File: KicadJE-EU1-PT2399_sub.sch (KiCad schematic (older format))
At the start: 49 parts, among them J201 In, J202 Out, P201 HEADER_2x5_Doepfer, Q201 BC337, Q202 PZT2222A, Q203 PZT2222A, U202 PT2399

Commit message: argh Kicad not stable
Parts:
- D204: footprint Diode_SMD:D_MELF-RM10_Universal_Handsoldering -> Diode_SMD:D_MiniMELF
- RV202: footprint Potentiometer_THT:Potentiometer_Alps_RK09K_Single_Vertical -> Potentiometer_THT:Potentiometer_China_RK09_Single_Vertical_AJ
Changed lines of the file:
@@
 F 0 "D204" V 4004 1704 50  0000 L CNN
 F 1 "5v6" V 4095 1704 50  0000 L CNN
-F 2 "Diode_SMD:D_MELF-RM10_Universal_Handsoldering" H 4050 1625 50  0001 C CNN
+F 2 "Diode_SMD:D_MiniMELF" H 4050 1625 50  0001 C CNN
 F 3 "~" H 4050 1625 50  0001 C CNN
 	1    4050 1625
@@
 F 0 "RV202" H 2380 5071 50  0000 R CNN
 F 1 "20k" H 2380 4980 50  0000 R CNN
-F 2 "Potentiometer_THT:Potentiometer_Alps_RK09K_Single_Vertical" H 2450 5025 50  0001 C CNN
+F 2 "Potentiometer_THT:Potentiometer_China_RK09_Single_Vertical_AJ" H 2450 5025 50  0001 C CNN
 F 3 "~" H 2450 5025 50  0001 C CNN
 	1    2450 5025

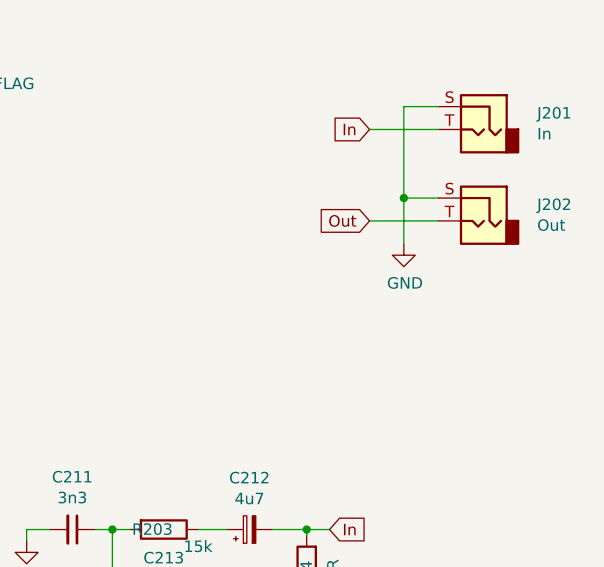
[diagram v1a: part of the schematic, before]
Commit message: Components placed on PT2399
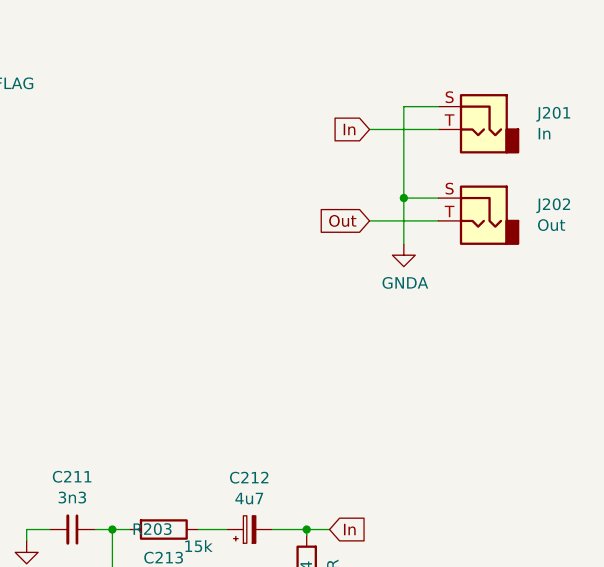
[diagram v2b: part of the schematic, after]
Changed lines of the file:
@@
 Wire Wire Line
 	6675 1200 6675 1600
-$Comp
-L power:GND #PWR?
-U 1 1 5C68B7E3
-P 6675 1800
-AR Path="/5C68B7E3" Ref="#PWR?"  Part="1"
-AR Path="/5D60ED9A/5C68B7E3" Ref="#PWR0205"  Part="1"
-F 0 "#PWR0205" H 6675 1550 50  0001 C CNN
-F 1 "GND" H 6680 1627 50  0000 C CNN
-F 2 "" H 6675 1800 50  0001 C CNN
-F 3 "" H 6675 1800 50  0001 C CNN
-	1    6675 1800
-	1    0    0    -1
-$EndComp
 Text GLabel 6525 1300 0    50   Input ~ 0
 In
@@
 Wire Wire Line
 	1875 1450 2550 1450
+$Comp
+L power:GNDA #PWR?
+U 1 1 5C768062
+P 6675 1800
+F 0 "#PWR?" H 6675 1550 50  0001 C CNN
+F 1 "GNDA" H 6680 1627 50  0000 C CNN
+F 2 "" H 6675 1800 50  0001 C CNN
+F 3 "" H 6675 1800 50  0001 C CNN
+	1    6675 1800
+	1    0    0    -1
+$EndComp
 $EndSCHEMATC

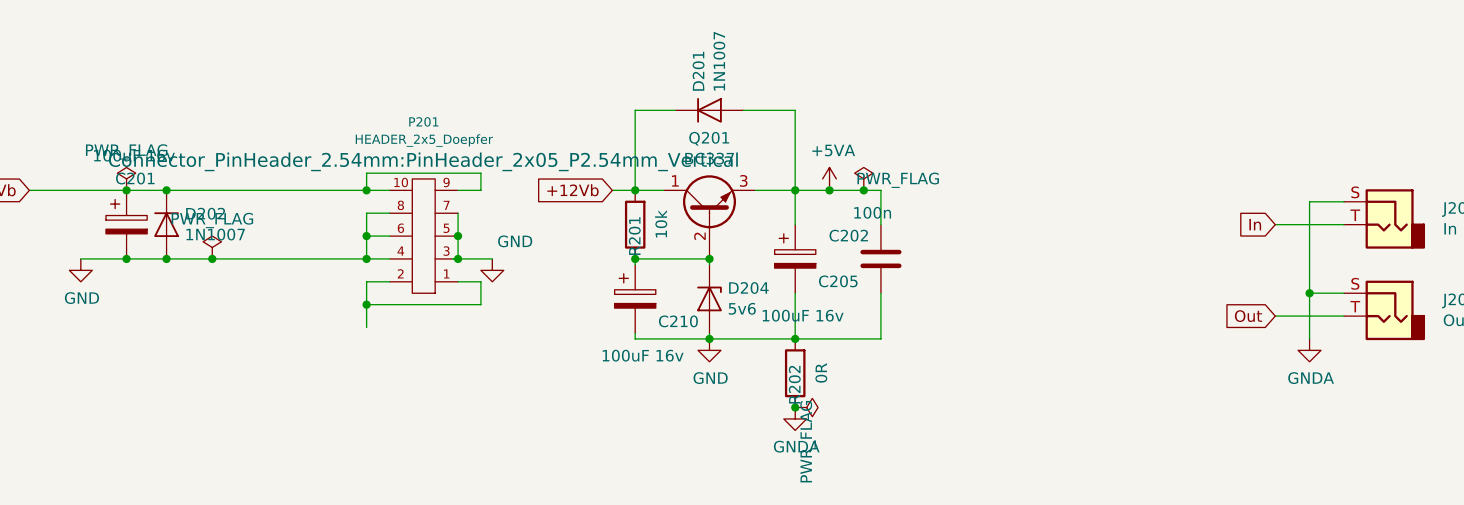
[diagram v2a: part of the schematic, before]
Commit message: Added 78L05 reg
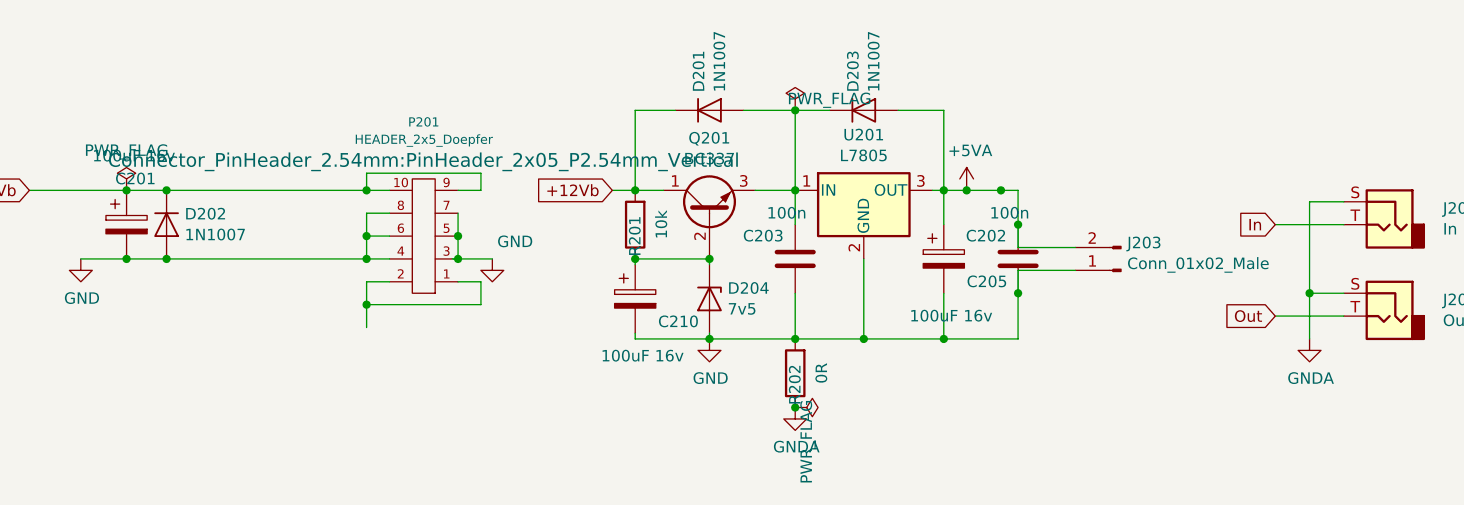
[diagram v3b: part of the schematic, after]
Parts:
- added C203: 100n, Capacitor_SMD:C_0805_2012Metric_Pad1.15x1.40mm_HandSolder, symbol Device:C
- added D203: 1N1007, Diode_SMD:D_SOD-123, symbol Device:D
- added J203: Conn_01x02_Male, Connector_PinHeader_2.54mm:PinHeader_1x02_P2.54mm_Vertical, symbol Connector:Conn_01x02_Male
- added U201: L7805, Package_TO_SOT_THT:TO-92, symbol Envelope-cache-2018-08-04-13-00-04:L7805
- D204: value 5v6 -> 7v5
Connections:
- wire segments 137 -> 149
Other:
- moved on the sheet: C202, C205
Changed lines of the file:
@@
 L Device:C C?
 U 1 1 5D62F383
-P 4800 1450
+P 5400 1450
 AR Path="/5D62F383" Ref="C?"  Part="1"
 AR Path="/5D60ED9A/5D62F383" Ref="C202"  Part="1"
-F 0 "C202" H 4850 1350 50  0000 L CNN
-F 1 "100n" H 4750 1250 50  0000 L CNN
-F 2 "Capacitor_SMD:C_0805_2012Metric_Pad1.15x1.40mm_HandSolder" H 4838 1300 50  0001 C CNN
-F 3 "~" H 4800 1450 50  0001 C CNN
-	1    4800 1450
+F 0 "C202" H 5450 1350 50  0000 L CNN
+F 1 "100n" H 5350 1250 50  0000 L CNN
+F 2 "Capacitor_SMD:C_0805_2012Metric_Pad1.15x1.40mm_HandSolder" H 5438 1300 50  0001 C CNN
+F 3 "~" H 5400 1450 50  0001 C CNN
+	1    5400 1450
 	-1   0    0    1
 $EndComp
@@
 	1    0    0    -1
 $EndComp
-$Comp
-L power:PWR_FLAG #FLG?
-U 1 1 5D62F3D0
-P 1875 1450
-AR Path="/5D62F3D0" Ref="#FLG?"  Part="1"
-AR Path="/5D60ED9A/5D62F3D0" Ref="#FLG0203"  Part="1"
-F 0 "#FLG0203" H 1875 1525 50  0001 C CNN
-F 1 "PWR_FLAG" H 1875 1624 50  0000 C CNN
-F 2 "" H 1875 1450 50  0001 C CNN
-F 3 "~" H 1875 1450 50  0001 C CNN
-	1    1875 1450
-	1    0    0    -1
-$EndComp
 Text GLabel 1075 1150 0    50   Input ~ 0
 +12Vb
@@
 L Device:CP C?
 U 1 1 5D645B0A
-P 4425 1450
+P 5075 1450
 AR Path="/5D645B0A" Ref="C?"  Part="1"
 AR Path="/5D60ED9A/5D645B0A" Ref="C205"  Part="1"
-F 0 "C205" H 4525 1350 50  0000 L CNN
-F 1 "100uF 16v" H 4275 1200 50  0000 L CNN
-F 2 "Capacitor_THT:CP_Radial_D5.0mm_P2.50mm" H 4463 1300 50  0001 C CNN
-F 3 "~" H 4425 1450 50  0001 C CNN
-	1    4425 1450
+F 0 "C205" H 5175 1350 50  0000 L CNN
+F 1 "100uF 16v" H 4925 1200 50  0000 L CNN
+F 2 "Capacitor_THT:CP_Radial_D5.0mm_P2.50mm" H 5113 1300 50  0001 C CNN
+F 3 "~" H 5075 1450 50  0001 C CNN
+	1    5075 1450
 	1    0    0    -1
 $EndComp
@@
 P 4050 1625
 F 0 "D204" V 4004 1704 50  0000 L CNN
-F 1 "5v6" V 4095 1704 50  0000 L CNN
+F 1 "7v5" V 4095 1704 50  0000 L CNN
 F 2 "Diode_SMD:D_MiniMELF" H 4050 1625 50  0001 C CNN
 F 3 "~" H 4050 1625 50  0001 C CNN
@@
 L power:+5VA #PWR0201
 U 1 1 5D64AB64
-P 4575 1150
-F 0 "#PWR0201" H 4575 1000 50  0001 C CNN
-F 1 "+5VA" H 4590 1323 50  0000 C CNN
-F 2 "" H 4575 1150 50  0001 C CNN
-F 3 "" H 4575 1150 50  0001 C CNN
-	1    4575 1150
+P 5175 1150
+F 0 "#PWR0201" H 5175 1000 50  0001 C CNN
+F 1 "+5VA" H 5190 1323 50  0000 C CNN
+F 2 "" H 5175 1150 50  0001 C CNN
+F 3 "" H 5175 1150 50  0001 C CNN
+	1    5175 1150
 	1    0    0    -1
 $EndComp
@@
 L power:PWR_FLAG #FLG?
 U 1 1 5D64AB9E
-P 4725 1150
+P 4425 800
 AR Path="/5D64AB9E" Ref="#FLG?"  Part="1"
 AR Path="/5D60ED9A/5D64AB9E" Ref="#FLG0202"  Part="1"
-F 0 "#FLG0202" H 4725 1225 50  0001 C CNN
-F 1 "PWR_FLAG" H 4875 1200 50  0000 C CNN
-F 2 "" H 4725 1150 50  0001 C CNN
-F 3 "~" H 4725 1150 50  0001 C CNN
-	1    4725 1150
+F 0 "#FLG0202" H 4425 875 50  0001 C CNN
+F 1 "PWR_FLAG" H 4575 850 50  0000 C CNN
+F 2 "" H 4425 800 50  0001 C CNN
+F 3 "~" H 4425 800 50  0001 C CNN
+	1    4425 800
 	1    0    0    -1
 $EndComp
@@
 	3625 1150 3725 1150
 Wire Wire Line
-	4425 1150 4575 1150
-Connection ~ 4575 1150
-Wire Wire Line
-	4575 1150 4725 1150
+	5025 1150 5075 1150
+Connection ~ 5175 1150
+Wire Wire Line
+	5175 1150 5325 1150
 $Comp
 L Audio:PT2399 U202
@@
 	1075 1150 1500 1150
 Wire Wire Line
-	4425 1800 4800 1800
-Wire Wire Line
-	4800 1800 4800 1600
-Wire Wire Line
 	1675 1150 2550 1150
 Wire Wire Line
-	1675 1450 1875 1450
-Wire Wire Line
-	4800 1300 4800 1150
-Wire Wire Line
-	4800 1150 4725 1150
-Connection ~ 4725 1150
-Connection ~ 1875 1450
-Wire Wire Line
-	1875 1450 2550 1450
-$Comp
-L power:GNDA #PWR?
+	5400 1150 5325 1150
+Connection ~ 5325 1150
+$Comp
+L power:GNDA #PWR0102
 U 1 1 5C768062
 P 6675 1800
-F 0 "#PWR?" H 6675 1550 50  0001 C CNN
+F 0 "#PWR0102" H 6675 1550 50  0001 C CNN
 F 1 "GNDA" H 6680 1627 50  0000 C CNN
 F 2 "" H 6675 1800 50  0001 C CNN
@@
 	1    0    0    -1
 $EndComp
+$Comp
+L Connector:Conn_01x02_Male J203
+U 1 1 5C76AAB7
+P 5850 1500
+F 0 "J203" H 5823 1380 50  0000 R CNN
+F 1 "Conn_01x02_Male" H 5823 1471 50  0000 R CNN
+F 2 "Connector_PinHeader_2.54mm:PinHeader_1x02_P2.54mm_Vertical" H 5850 1500 50  0001 C CNN
+F 3 "~" H 5850 1500 50  0001 C CNN
+	1    5850 1500
+	-1   0    0    1
+$EndComp
+$Comp
+L Envelope-cache-2018-08-04-13-00-04:L7805 U201
+U 1 1 5C76AC9D
+P 4725 1150
+F 0 "U201" H 4725 1392 50  0000 C CNN
+F 1 "L7805" H 4725 1301 50  0000 C CNN
+F 2 "Package_TO_SOT_THT:TO-92" H 4750 1000 50  0001 L CIN
+F 3 "" H 4725 1100 50  0001 C CNN
+	1    4725 1150
+	1    0    0    -1
+$EndComp
+Wire Wire Line
+	5075 1300 5075 1150
+Connection ~ 5075 1150
+Wire Wire Line
+	5075 1150 5175 1150
+Wire Wire Line
+	5075 1600 5075 1800
+Connection ~ 5075 1800
+Wire Wire Line
+	5075 1800 5400 1800
+Wire Wire Line
+	4425 1800 4725 1800
+$Comp
+L Device:C C?
+U 1 1 5C78460D
+P 4425 1450
+AR Path="/5C78460D" Ref="C?"  Part="1"
+AR Path="/5D60ED9A/5C78460D" Ref="C203"  Part="1"
+F 0 "C203" H 4475 1350 50  0000 L CNN
+F 1 "100n" H 4375 1250 50  0000 L CNN
+F 2 "Capacitor_SMD:C_0805_2012Metric_Pad1.15x1.40mm_HandSolder" H 4463 1300 50  0001 C CNN
+F 3 "~" H 4425 1450 50  0001 C CNN
+	1    4425 1450
+	-1   0    0    1
+$EndComp
+Wire Wire Line
+	4725 1450 4725 1800
+Connection ~ 4725 1800
+Wire Wire Line
+	4725 1800 5075 1800
+Wire Wire Line
+	5400 1400 5650 1400
+Wire Wire Line
+	5400 1150 5400 1300
+Connection ~ 5400 1300
+Wire Wire Line
+	5400 1300 5400 1400
+Wire Wire Line
+	5650 1500 5400 1500
+Wire Wire Line
+	5400 1500 5400 1600
+Connection ~ 5400 1600
+Wire Wire Line
+	5400 1600 5400 1800
+$Comp
+L Device:D D?
+U 1 1 5C794D49
+P 4725 800
+AR Path="/5C794D49" Ref="D?"  Part="1"
+AR Path="/5D60ED9A/5C794D49" Ref="D203"  Part="1"
+F 0 "D203" V 4679 879 50  0000 L CNN
+F 1 "1N1007" V 4770 879 50  0000 L CNN
+F 2 "Diode_SMD:D_SOD-123" H 4725 800 50  0001 C CNN
+F 3 "~" H 4725 800 50  0001 C CNN
+	1    4725 800
+	1    0    0    -1
+$EndComp
+Wire Wire Line
+	4425 800  4575 800
+Connection ~ 4425 800
+Wire Wire Line
+	5075 1150 5075 800
+Wire Wire Line
+	5075 800  4875 800
+Wire Wire Line
+	1675 1450 2550 1450
 $EndSCHEMATC

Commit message: Replace 16pin doepfer with 10pin on EU3
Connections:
- wire segments 149 -> 148
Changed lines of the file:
@@
 	5025 1150 5075 1150
 Connection ~ 5175 1150
-Wire Wire Line
-	5175 1150 5325 1150
 $Comp
 L Audio:PT2399 U202
@@
 Wire Wire Line
 	1675 1150 2550 1150
-Wire Wire Line
-	5400 1150 5325 1150
-Connection ~ 5325 1150
 $Comp
 L power:GNDA #PWR0102
@@
 Wire Wire Line
 	1675 1450 2550 1450
+Wire Wire Line
+	5175 1150 5400 1150
 $EndSCHEMATC
